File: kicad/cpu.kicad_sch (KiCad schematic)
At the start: 0 parts

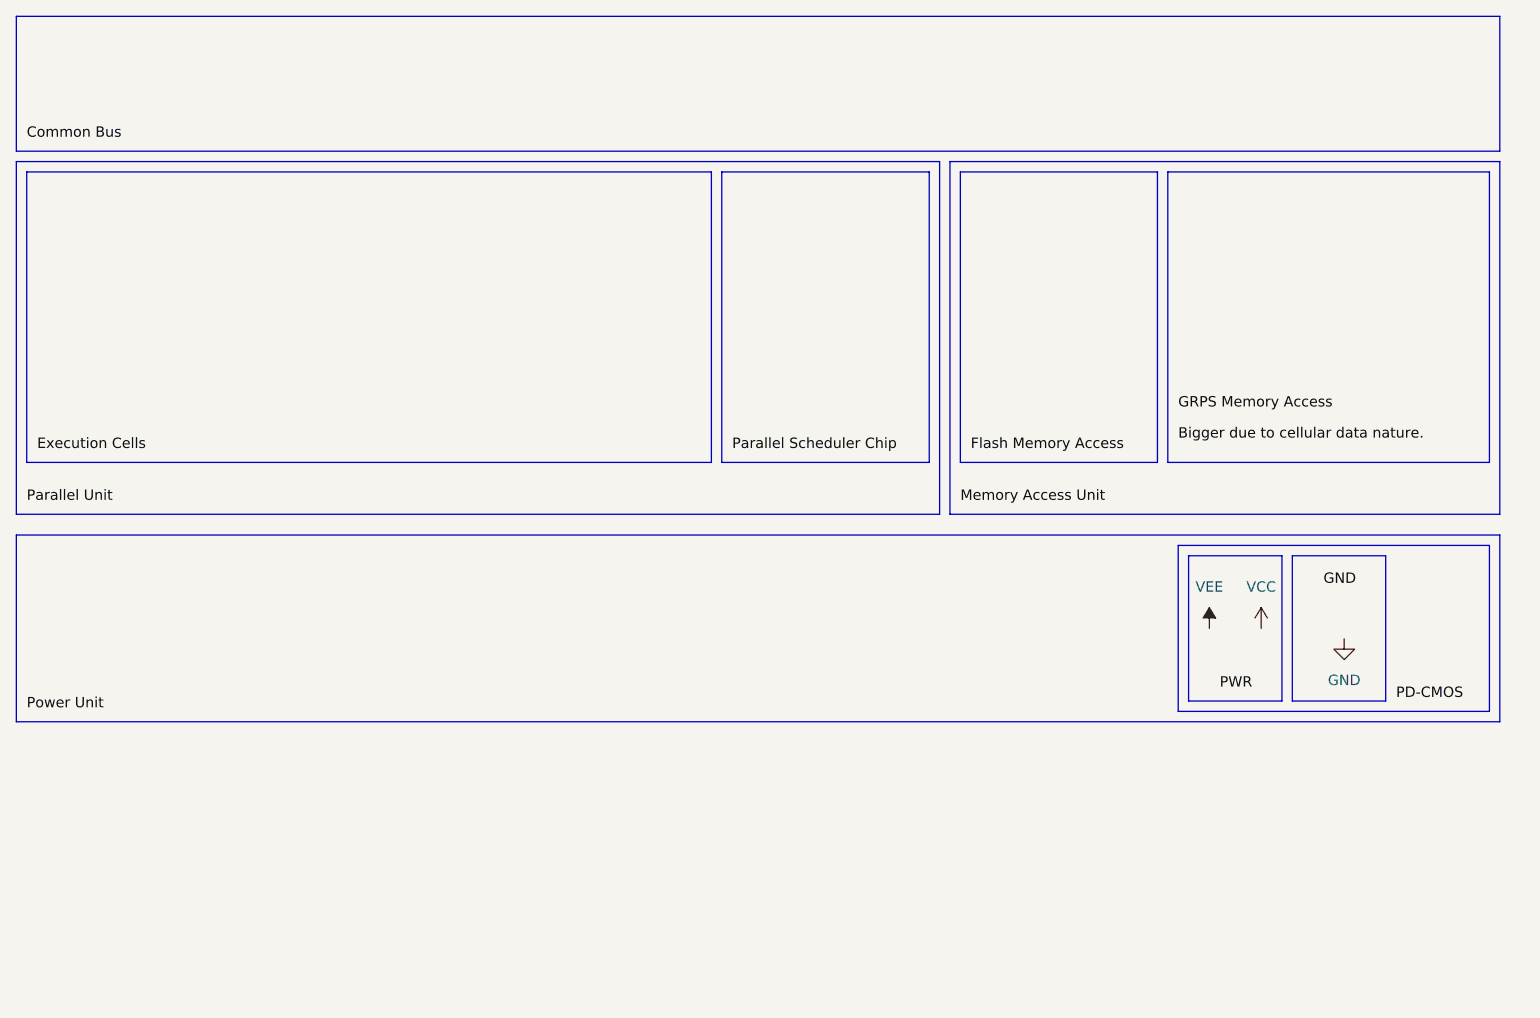
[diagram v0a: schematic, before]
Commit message: [CHORE] src: Rework the schematic to include bus, additional units for DMA, and caches.
Signed-off-by: Amlal El Mahrouss <amlal@nekernel.org>
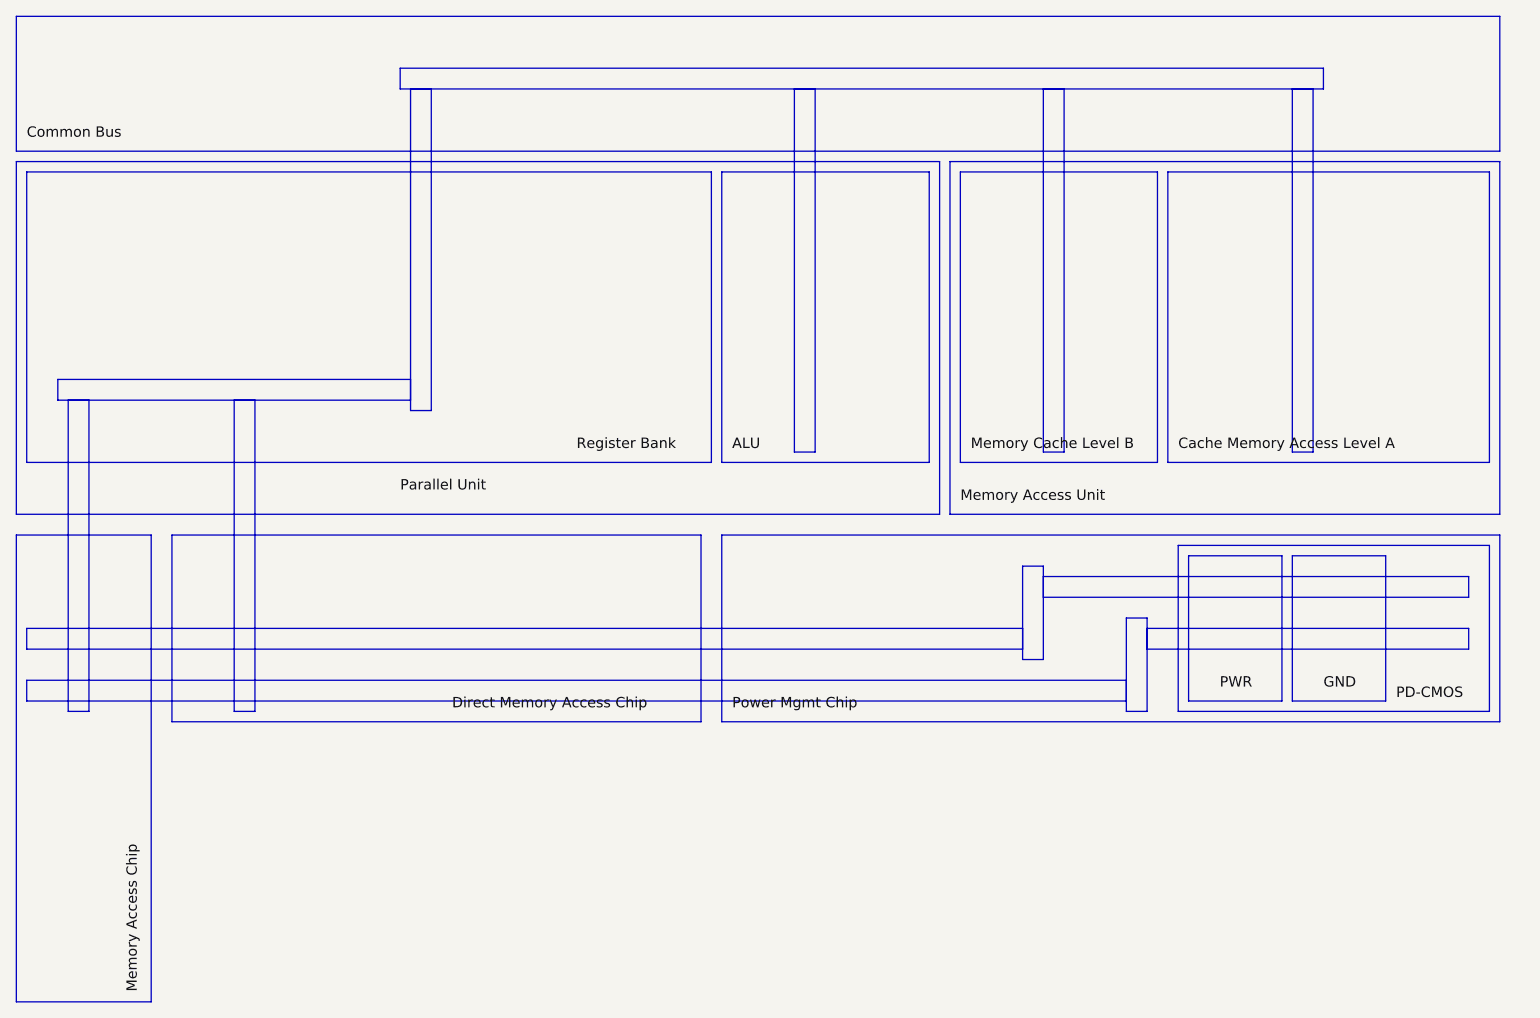
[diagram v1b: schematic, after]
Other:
- company: Amlal El Mahrouss -> A.E.
- title: Howard -> Overlake
